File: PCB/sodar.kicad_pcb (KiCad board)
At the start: 2 copper layers, 71 parts, among them J1 Screw_Terminal_01x02, J2 Conn_02x12_Counter_Clockwise, J3 Conn_01x02, U1 TC78H621FNG, U10 TC78H621FNG, U2 TC78H621FNG, U3 TC78H621FNG, U4 TC78H621FNG, U5 TC78H621FNG, U6 TC78H621FNG, U7 TC78H621FNG, U8 TC78H621FNG, U9 TC78H621FNG

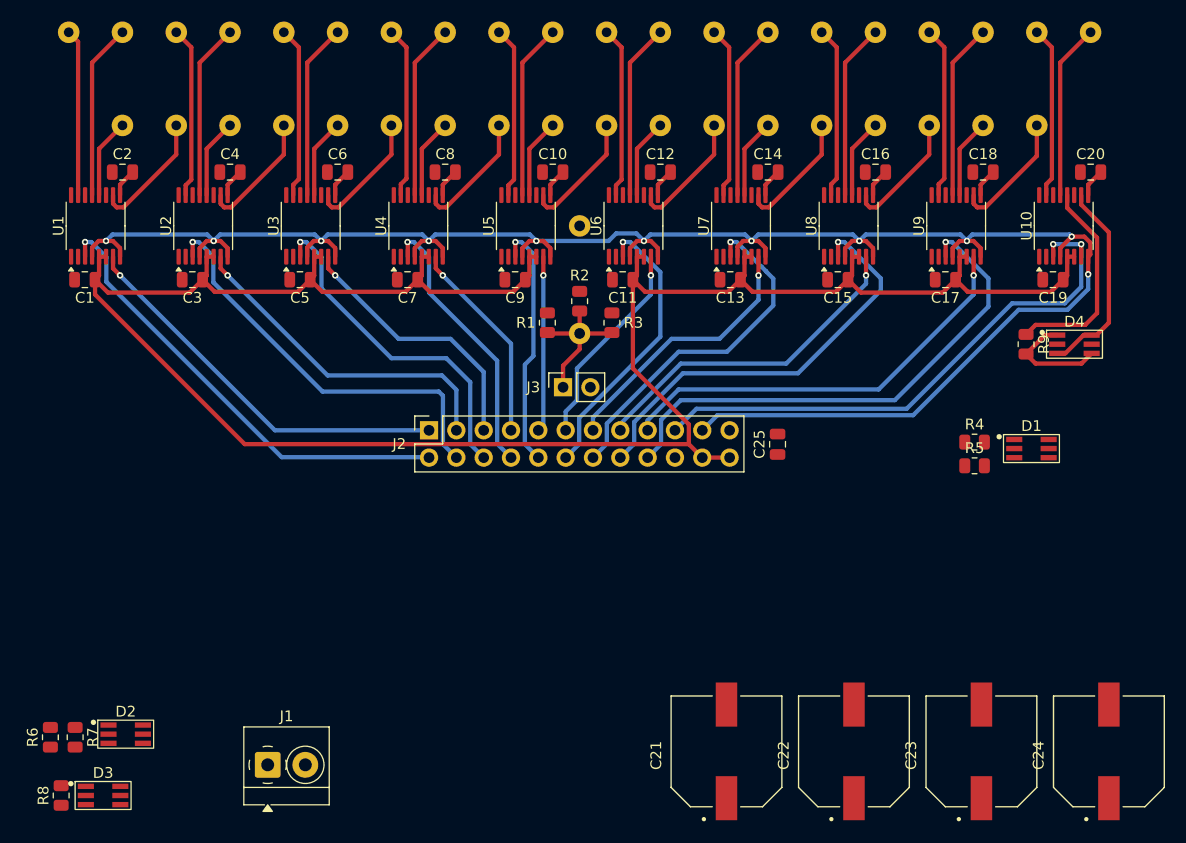
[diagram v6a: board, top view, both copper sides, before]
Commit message: Routed VDrvie screw terminal & caps
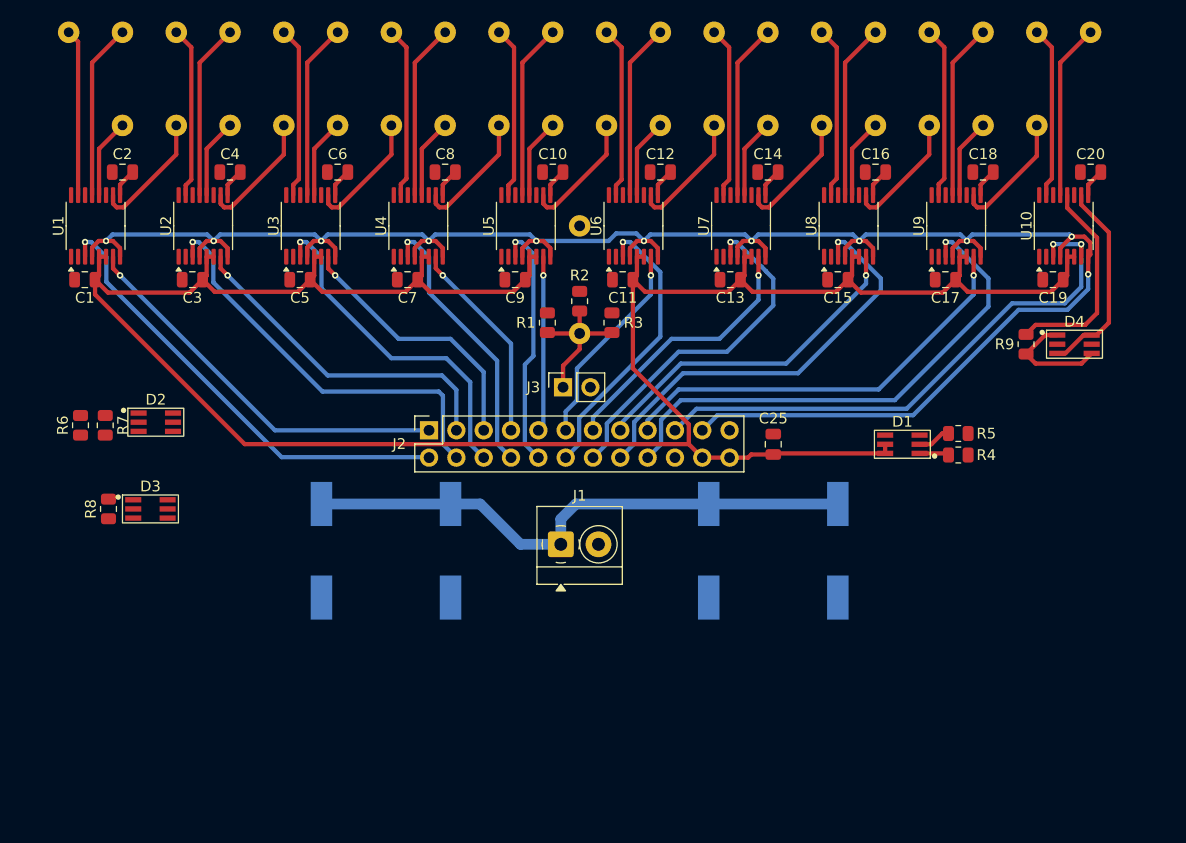
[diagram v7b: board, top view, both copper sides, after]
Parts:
- C21, C22, C23, C24: moved to B.Cu
- moved C24 75.5 mm to (126.0, 83.2), turned to -90 degrees
- moved C23 52.8 mm to (138.0, 83.2), turned to -90 degrees
- moved J1 34.1 mm to (148.2, 82.6)
- moved D2 29.1 mm to (110.6, 71.2)
- moved R6 29.1 mm to (103.6, 71.5)
- moved R7 29.1 mm to (105.9, 71.5)
- moved R8 27.0 mm to (106.2, 79.3)
- moved D3 27.0 mm to (110.1, 79.3)
- moved C22 23.0 mm to (162.0, 83.2), turned to -90 degrees
- moved C21 21.3 mm to (174.0, 83.2), turned to -90 degrees
- moved D1 12.0 mm to (180.0, 73.3), turned to 180 degrees
- moved R5 3.36 mm to (185.2, 72.3), turned to 180 degrees
- moved R4 1.93 mm to (185.2, 74.3), turned to 180 degrees
- moved C25 0.40 mm to (168.0, 73.3)
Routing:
- net Vdrive: track 26.2 -> 78.7 mm
- net +3V3: track 201.1 -> 216.6 mm
- net Net-(D1-G-): track 0.00 -> 3.10 mm
- net Net-(D1-B-): track 0.00 -> 2.75 mm

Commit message: Finished VDrive route & LEDs
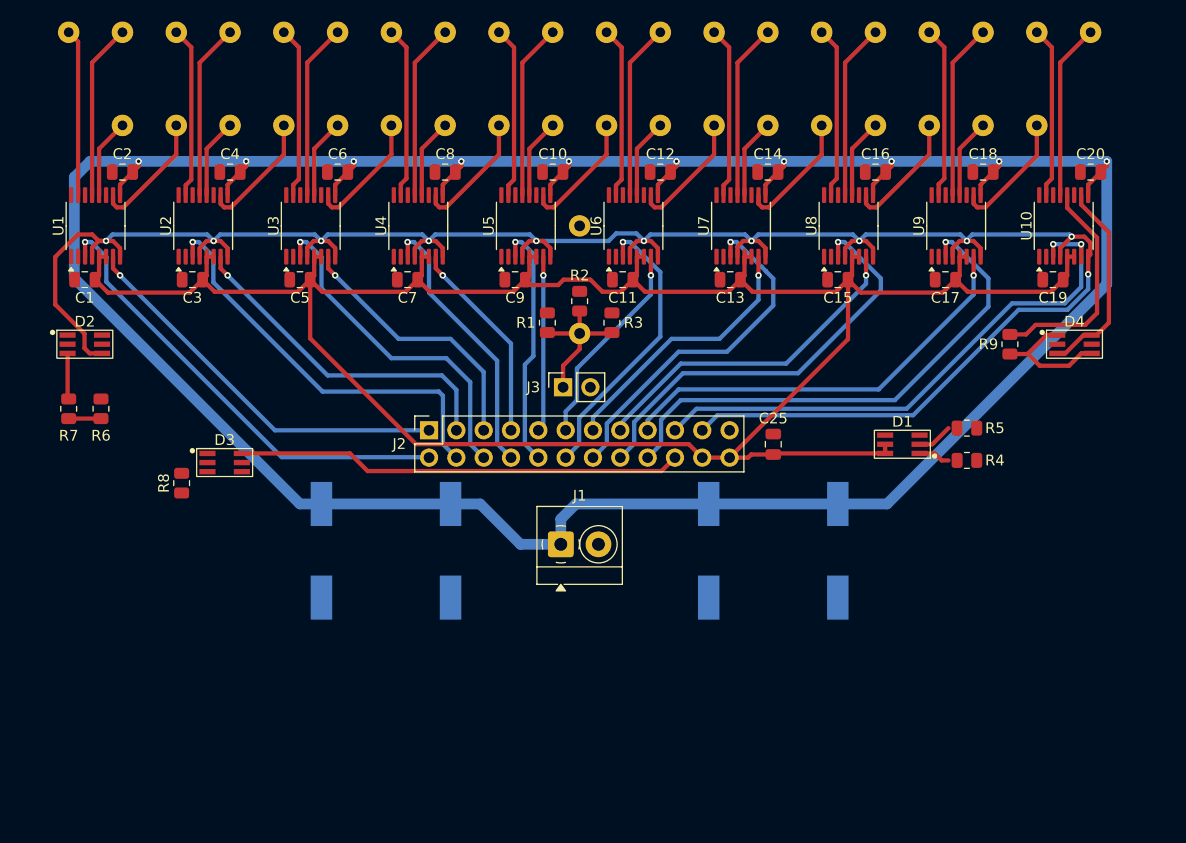
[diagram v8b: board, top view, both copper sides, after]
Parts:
- moved D2 9.80 mm to (104.0, 64.0)
- moved D3 8.14 mm to (117.0, 75.0)
- moved R8 7.21 mm to (113.0, 76.9)
- moved R7 3.73 mm to (102.5, 70.0), turned to 90 degrees
- moved R6 2.44 mm to (105.5, 70.0), turned to -90 degrees
- moved R9 1.50 mm to (190.0, 64.0)
- moved R4 0.94 mm to (186.0, 74.8)
- moved R5 0.94 mm to (186.0, 71.8)
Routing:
- net Vdrive: track 78.7 -> 273.5 mm, vias 0 -> 10
- net LED: track 0.00 -> 41.5 mm
- net EN: track 186.9 -> 204.2 mm
- net Net-(D2-R-): track 0.00 -> 4.28 mm
- net Net-(R6-Pad2): track 0.00 -> 3.00 mm
- net +3V3: track 216.6 -> 214.0 mm
- net Net-(D4-B-): track 10.5 -> 12.0 mm
- net PHA_LED1: track 19.5 -> 21.0 mm
